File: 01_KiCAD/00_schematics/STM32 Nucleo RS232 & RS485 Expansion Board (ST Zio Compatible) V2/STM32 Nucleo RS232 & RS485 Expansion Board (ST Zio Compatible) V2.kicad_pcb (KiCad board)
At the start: 4 copper layers, 70 x 133.4 mm, 190 parts, among them CN10 Conn_02x17_Odd_Even, CN7 Conn_02x10_Odd_Even, CN8 Conn_02x08_Odd_Even, CN9 Conn_02x15_Odd_Even, IC1 REG103GA-A, J1 1190299, J10 DIR, J11 TERM_TX, J12 TERM_RX, J13 SLR, J2 CONN D-SUB PLUG 9POS TH, J3 TCVR_PWR, J4 TX_LED, J5 RX_LED, J6 SW_ENA, J7 MODE0, J8 MODE1, J9 MODE2, Q1 BSS84, Q2 BSS84, U1 TPS2117DRLR, U10 SN74LVC2G14DBV, U11 SN74LVC2G14DBV, U2 THVD4431RHAR, U3 SN74LVC2G14DBV, U4 SN74LVC245ADBR, U5 SN74LVC2G14DBV, U6 SN74LVC2G14DBV, U7 SN74LVC2G14DBV, U8 SN74LVC2G14DBV, U9 SN74LVC2G14DBV

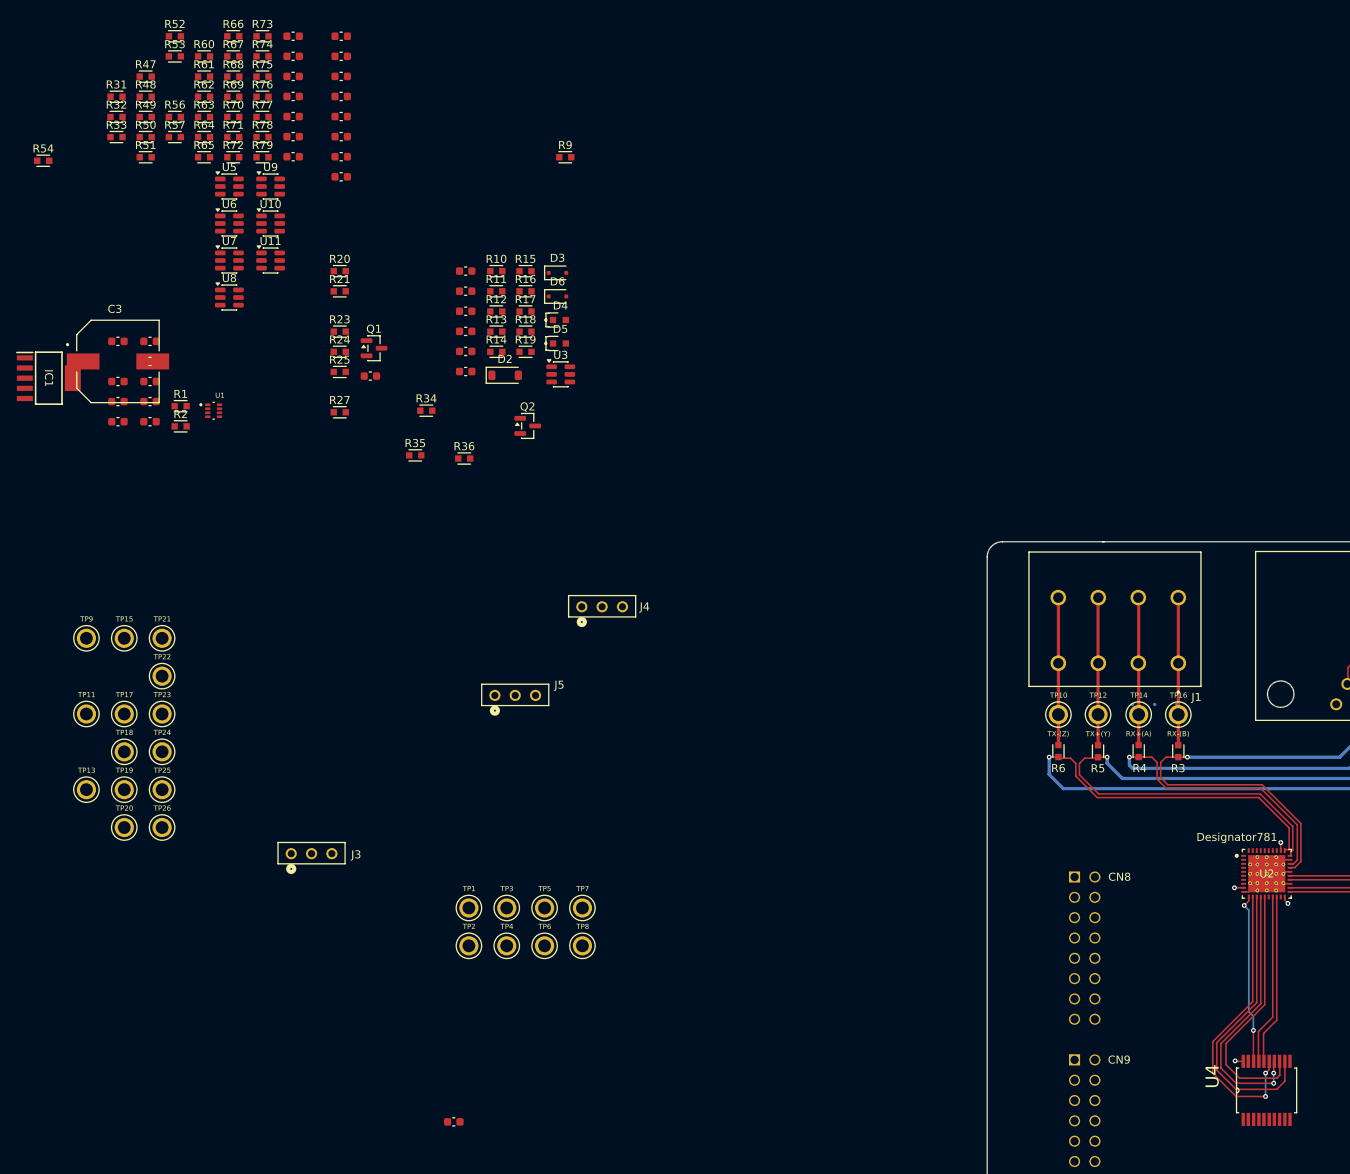
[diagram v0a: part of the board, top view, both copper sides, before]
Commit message: Capacitor change
Changed designator values for C1 t/m C7 so it is more logical on the sheet.
Changed capacittor C7 from 100µF to lower part of 47µF because of mechanical reasons. Old capacitor was too high and new capacitor of 47µ is just about 5-6mm in height
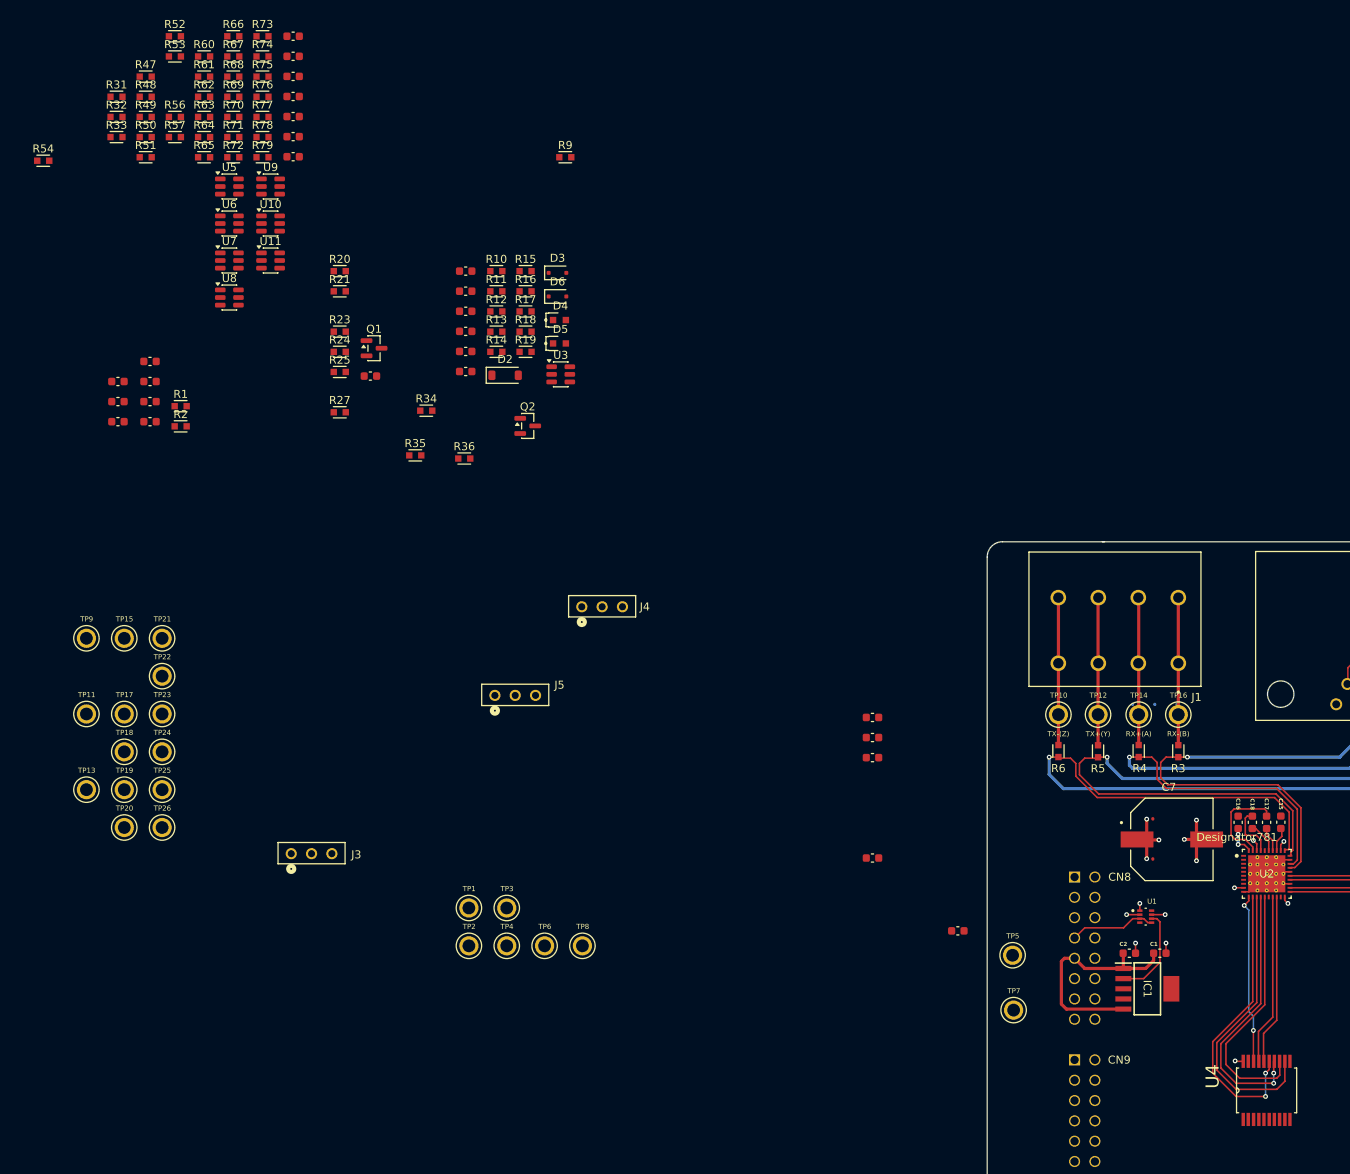
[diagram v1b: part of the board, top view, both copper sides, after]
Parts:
- C1: value 100nF -> 1µF
- C2: value 470nF -> 100nF
- C3: value 100µF -> 100nF; footprint EEEHD1H101P:CAP_EEEHD1H101P -> PCM_SparkFun-Capacitor:C_0603_1608Metric
- C4: value 100nF -> 10nF
- C5: value 10nF -> 100nF
- C6: value 1µF -> 470nF
- C7: value 100nF -> 47µF; footprint PCM_SparkFun-Capacitor:C_0603_1608Metric -> EEEHD1H101P:CAP_EEEHD1H101P
- moved IC1 157.1 mm to (56.8, 92.7)
- moved C15 148.4 mm to (73.5, 71.9), turned to 90 degrees
- moved C2 147.8 mm to (54.6, 88.3)
- moved C17 144.0 mm to (71.8, 71.9), turned to -90 degrees
- moved C16 142.7 mm to (68.2, 71.9), turned to 90 degrees
- moved C7 142.1 mm to (59.9, 74.0)
- moved C18 141.1 mm to (70.0, 71.9), turned to -90 degrees
- moved U1 132.6 mm to (56.6, 83.7)
- moved C3 126.8 mm to (33.2, 85.5)
- moved C12 108.0 mm to (22.5, 58.8)
- moved C13 108.0 mm to (22.5, 61.3)
- moved C14 108.0 mm to (22.5, 63.8)
- moved C19 108.0 mm to (22.5, 76.4)
- moved C1 90.7 mm to (58.4, 88.3)
- moved TP5 58.8 mm to (40.0, 88.5)
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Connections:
- C1 pad 1: 3V3_SYS -> ARDUINO_5V
- C2 pad 1: GND -> ARDUINO_5V
- C2 pad 2: 3V3_SYS -> GND
- C3 pad 1: 3V3_SYS -> 3V3_LDO
- C4 pad 1: 3V3_LDO -> Net-(U1-PR1)
- C5 pad 1: Net-(U1-PR1) -> 3V3_SYS
- C6 pad 1: ARDUINO_5V -> GND
- C6 pad 2: GND -> 3V3_SYS
- C7 pad 1: ARDUINO_5V -> 3V3_SYS
- U2 pad 42: GND -> (no net)
- U2 pad 43: GND -> (no net)
- U2 pad 44: GND -> (no net)
- U2 pad 45: GND -> (no net)
- U2 pad 46: GND -> (no net)
- U2 pad 47: GND -> (no net)
- U2 pad 48: GND -> (no net)
- U2 pad 49: GND -> (no net)
- U2 pad 50: GND -> (no net)
- U2 pad 51: GND -> (no net)
- U2 pad 52: GND -> (no net)
- U2 pad 53: GND -> (no net)
- U2 pad 54: GND -> (no net)
- U2 pad 55: GND -> (no net)
- U2 pad 56: GND -> (no net)
- U2 pad 57: GND -> (no net)
- U2 pad 58: GND -> (no net)
- U2 pad 59: GND -> (no net)
- U2 pad 60: GND -> (no net)
- U2 pad 61: GND -> (no net)
- U2 pad 62: GND -> (no net)
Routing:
- net ARDUINO_5V: track 0.00 -> 28.8 mm
- net 3V3_SYS: track 14.2 -> 26.9 mm, vias 4 -> 10
- net GND: track 15.1 -> 27.4 mm, vias 4 -> 10
- net Net-(U2-C2+): track 0.00 -> 12.1 mm
- net 3V3_LDO: track 0.00 -> 11.7 mm
- net NUCLEO_3V3: track 0.00 -> 10.8 mm
- net Net-(U2-C1+): track 0.00 -> 6.61 mm
- net Net-(U2-C1-): track 0.00 -> 4.15 mm
- net Net-(U2-V+): track 0.00 -> 3.88 mm, vias 0 -> 2
- net Net-(U2-V-): track 0.00 -> 3.08 mm
- net Net-(U2-C2-): track 0.00 -> 3.07 mm
- net /RS232 & RS485 Tranceiver/TX-: track 94.3 -> 95.4 mm
- net /RS232 & RS485 Tranceiver/RX+: track 69.7 -> 70.9 mm
- net /RS232 & RS485 Tranceiver/RX-: track 58.6 -> 59.8 mm
- net /RS232 & RS485 Tranceiver/TX+: track 83.0 -> 84.2 mm

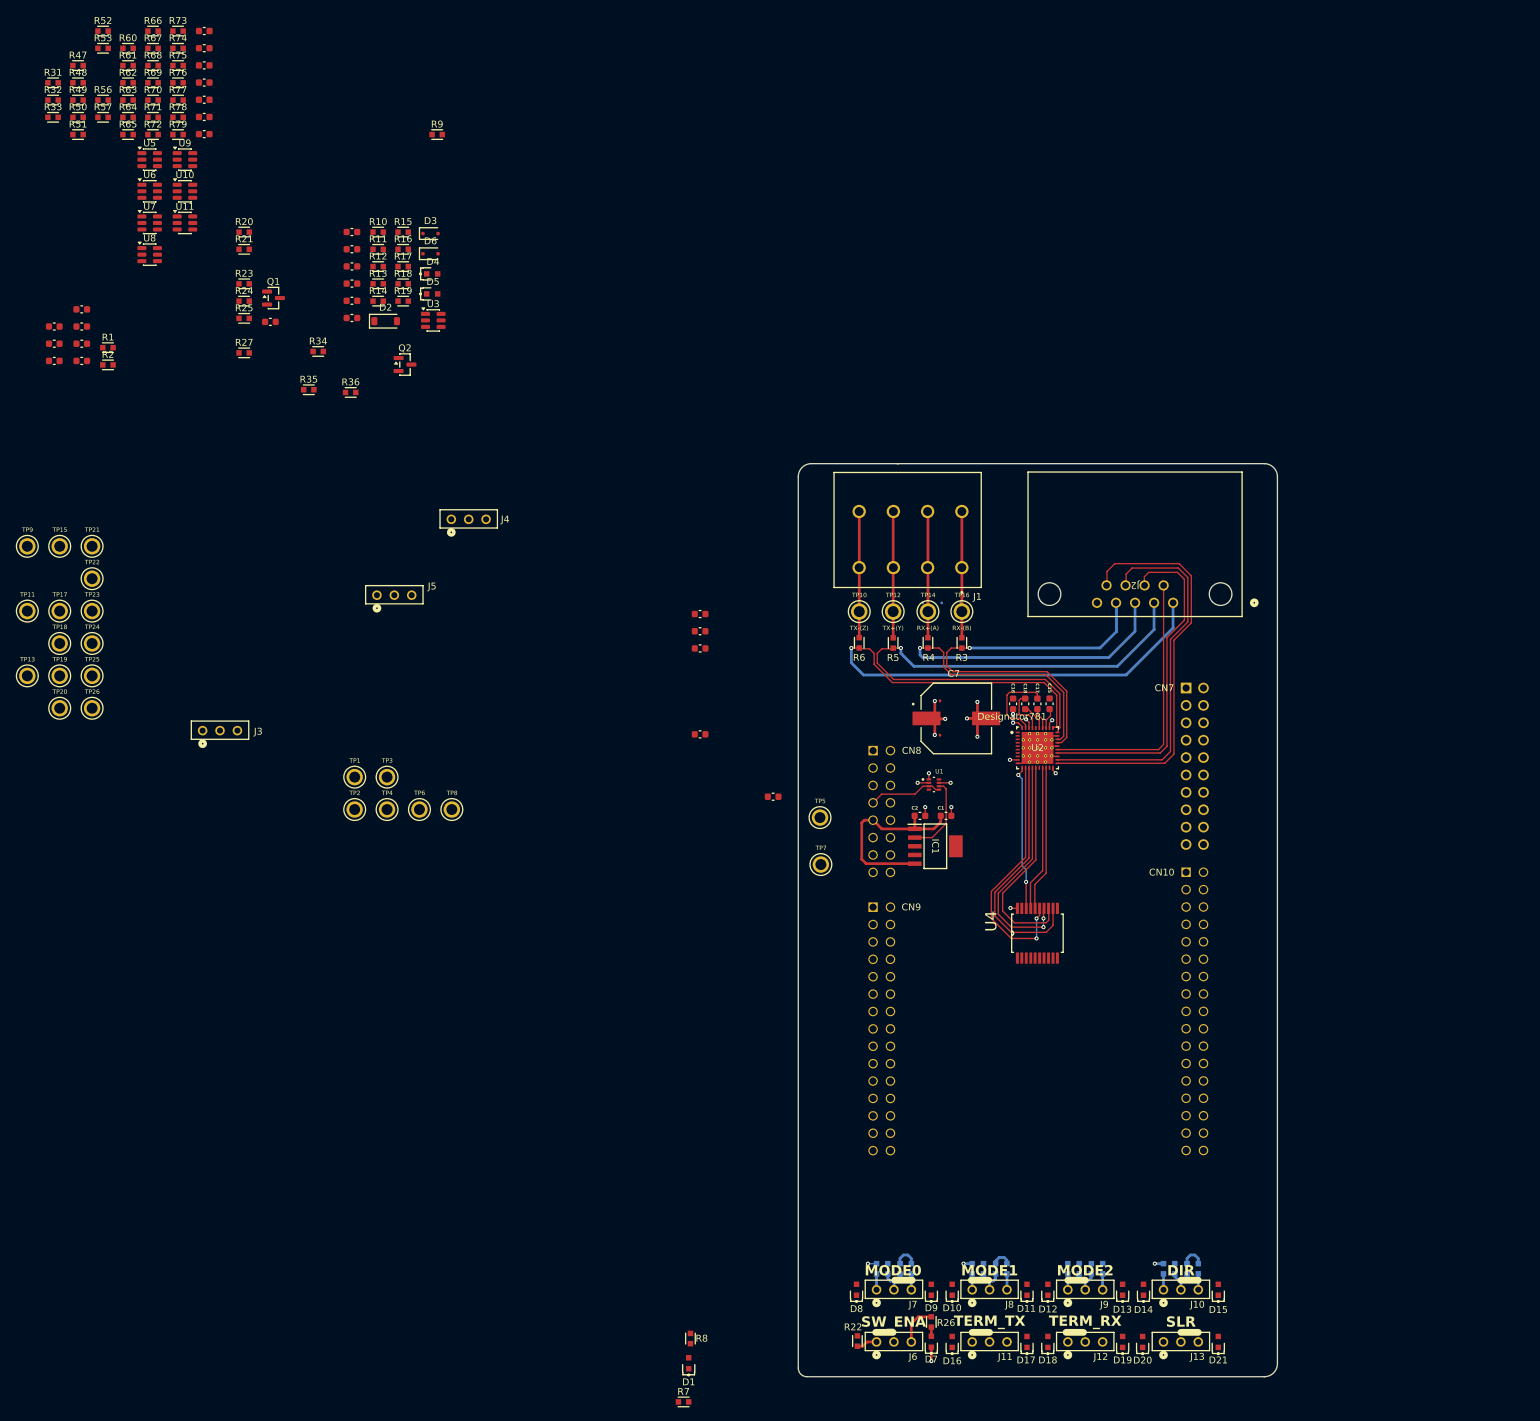
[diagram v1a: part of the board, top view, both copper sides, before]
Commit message: Updated footprints and added components to PCB
Added some additional components to the board. Changed the footprint of the 3-pin Jumper so the bottom silkscreen text doesnlt overlap with the Dual Schmidt Trigger IC's SN74LVC2G14
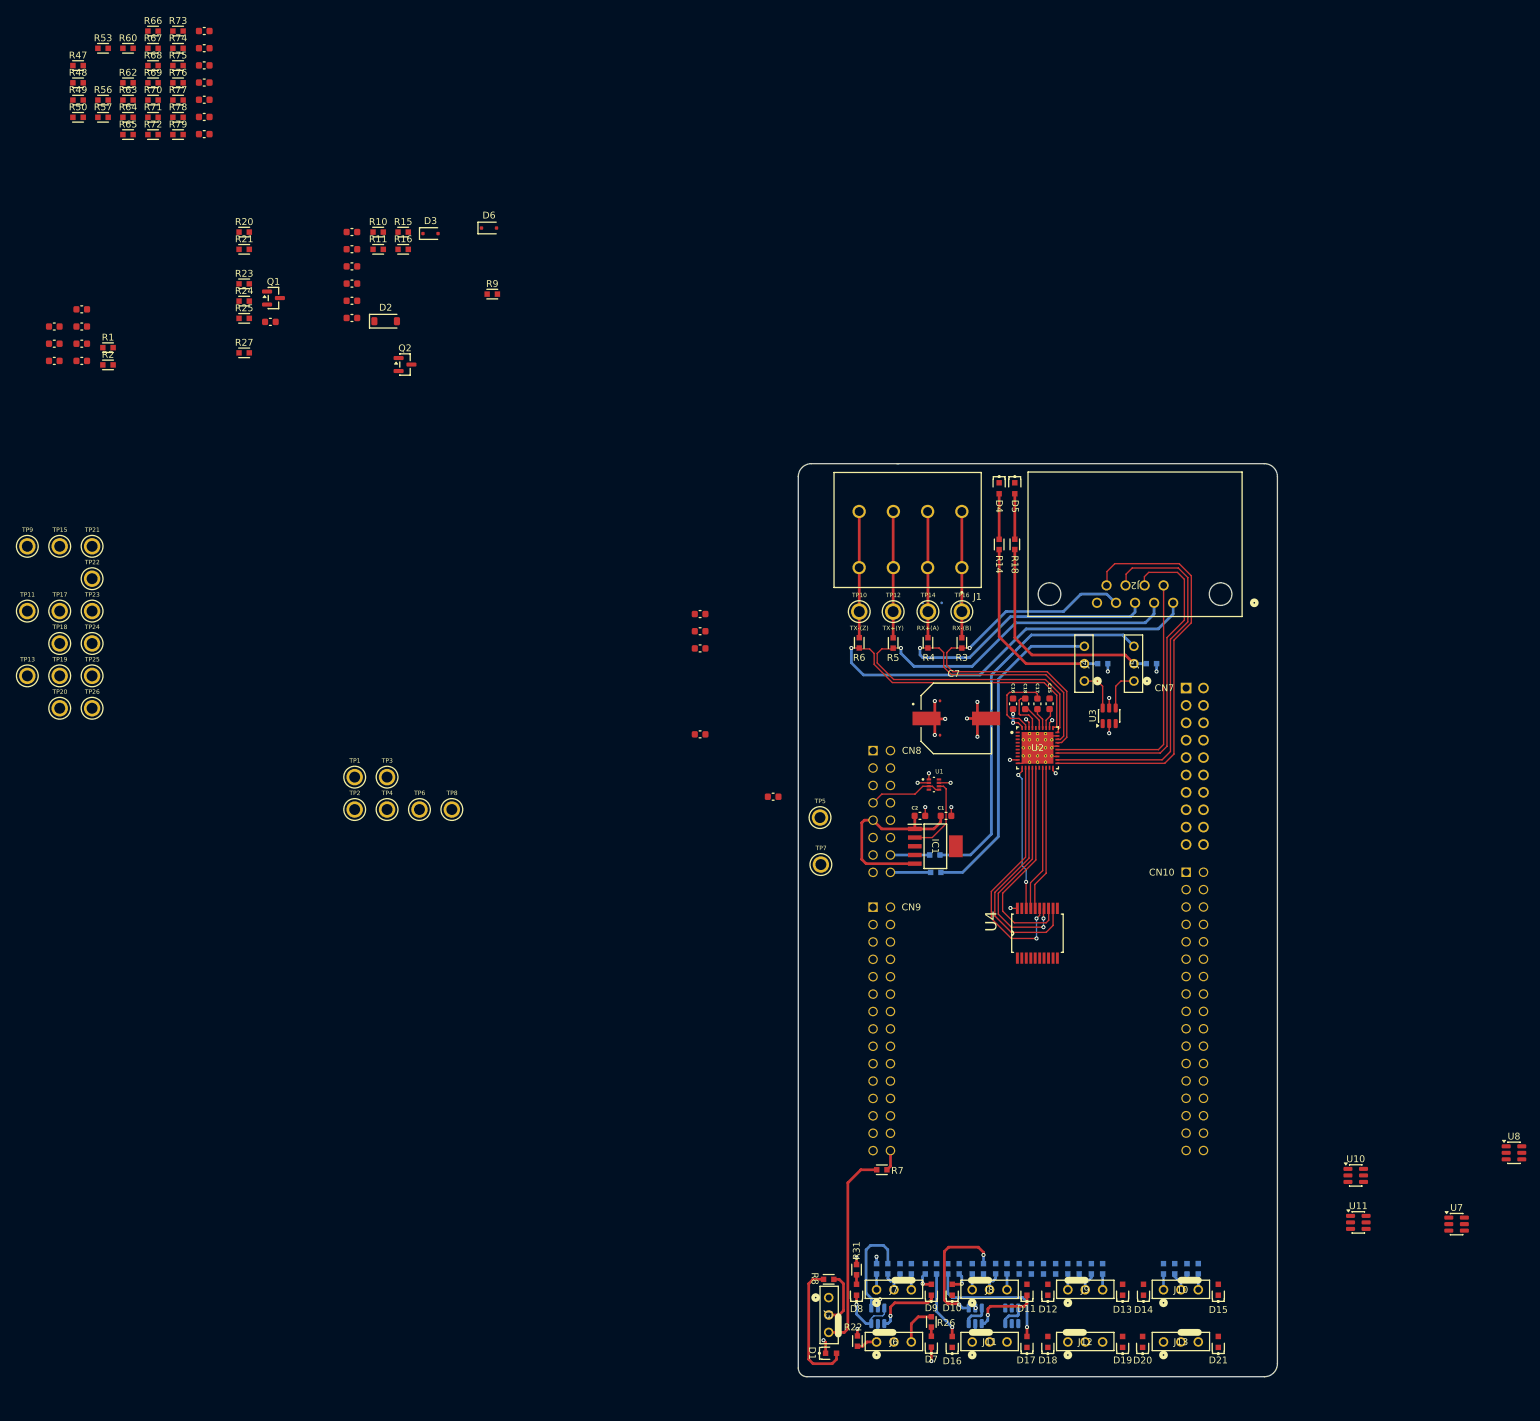
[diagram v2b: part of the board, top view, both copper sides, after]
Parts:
- J10, J11, J12, J13, J3, J4, J5, J6, J7, J8, J9: footprint HTSW-103-07-F-S:CON3_1X3_TU_TSW -> Samtec_Connector:Samtec HTSW-103-07-F-S
- R12, R13, R17, R19, R32, R33, R34, R35, R36, R51, R52, R61, U5, U6, U9: moved to B.Cu
- moved U7 240.4 mm to (133.0, 147.9)
- moved U8 238.6 mm to (141.4, 137.5)
- moved U11 225.1 mm to (118.6, 147.6)
- moved U10 223.4 mm to (118.2, 140.8)
- moved R61 219.7 mm to (70.9, 154.4), turned to -90 degrees
- moved R52 218.9 mm to (58.7, 154.4), turned to -90 degrees
- moved R33 214.0 mm to (60.3, 154.4), turned to 90 degrees
- moved R32 213.0 mm to (55.4, 154.4), turned to -90 degrees
- moved R31 209.3 mm to (45.3, 154.5), turned to 90 degrees
- moved R51 207.8 mm to (57.0, 154.4), turned to 90 degrees
- moved U9 207.6 mm to (68.0, 161.3), turned to -90 degrees
- moved U6 203.7 mm to (62.7, 161.3), turned to -90 degrees
- moved U5 199.6 mm to (48.5, 161.3), turned to -90 degrees
- moved R34 168.6 mm to (69.1, 154.4), turned to -90 degrees
- moved R35 167.3 mm to (72.6, 154.4), turned to 90 degrees
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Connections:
- net /Rx & Tx LED/TX_LED_DRV renamed Net-(J4-Pin_2)
- CN8 pad 14: MCU_TXLED_GPIO -> MCU_RXLED_GPIO
- CN8 pad 16: MCU_RXLED_GPIO -> MCU_TXLED_GPIO
- J4 pad 3: MCU_TXLED_GPIO -> Net-(J4-Pin_3)
- R12 pad 2: MCU_TXLED_GPIO -> Net-(J4-Pin_3)
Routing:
- net Net-(J5-Pin_3): track 0.00 -> 56.0 mm
- net Net-(J4-Pin_3): track 0.00 -> 48.1 mm
- net Net-(J5-Pin_2): track 0.00 -> 33.7 mm
- net Net-(J3-Pin_3): track 0.00 -> 29.3 mm
- net Net-(J4-Pin_2): track 0.00 -> 28.7 mm
- net Net-(D17-A): track 0.00 -> 19.9 mm, vias 0 -> 1
- net Net-(U6-1A): track 0.00 -> 19.1 mm, vias 0 -> 2
- net Net-(D1-A): track 0.00 -> 19.0 mm
- net Net-(U5-1A): track 0.00 -> 14.6 mm
- net Net-(D16-A): track 0.00 -> 10.1 mm, vias 0 -> 1
- net Net-(D9-K): track 0.00 -> 10.1 mm, vias 0 -> 1
- net Net-(D11-K): track 0.00 -> 10.0 mm, vias 0 -> 1
- net Net-(D8-K): track 0.00 -> 9.30 mm, vias 0 -> 1
- net /RS232 & RS485 Tranceiver/THVD_SHDN_N: track 0.00 -> 8.03 mm
- net Net-(D4-A): track 0.00 -> 6.65 mm
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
